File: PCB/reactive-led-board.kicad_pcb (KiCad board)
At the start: 2 copper layers, 2 parts, among them J1 Conn_01x03_Socket, U1 XIAO-ESP32-C5-SMD

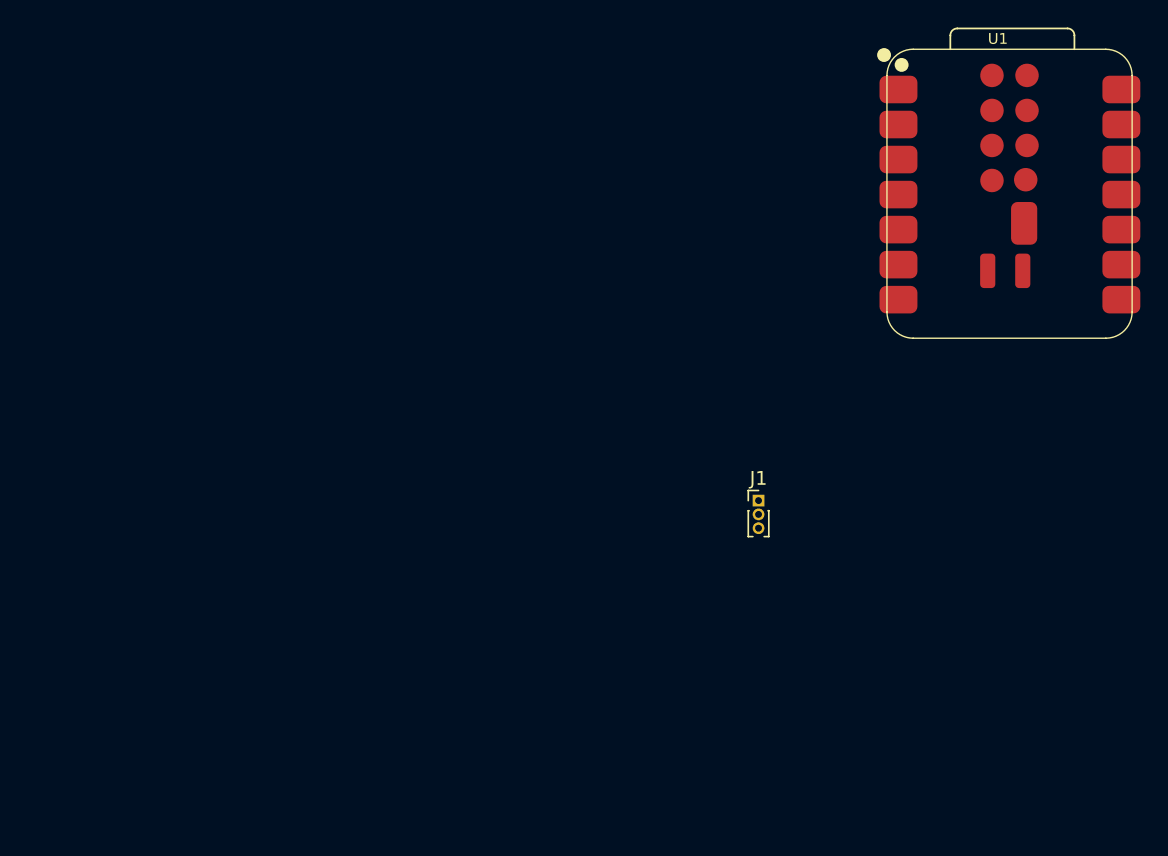
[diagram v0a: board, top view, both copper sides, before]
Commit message: routed the treaces and selected the parts i am going to use.
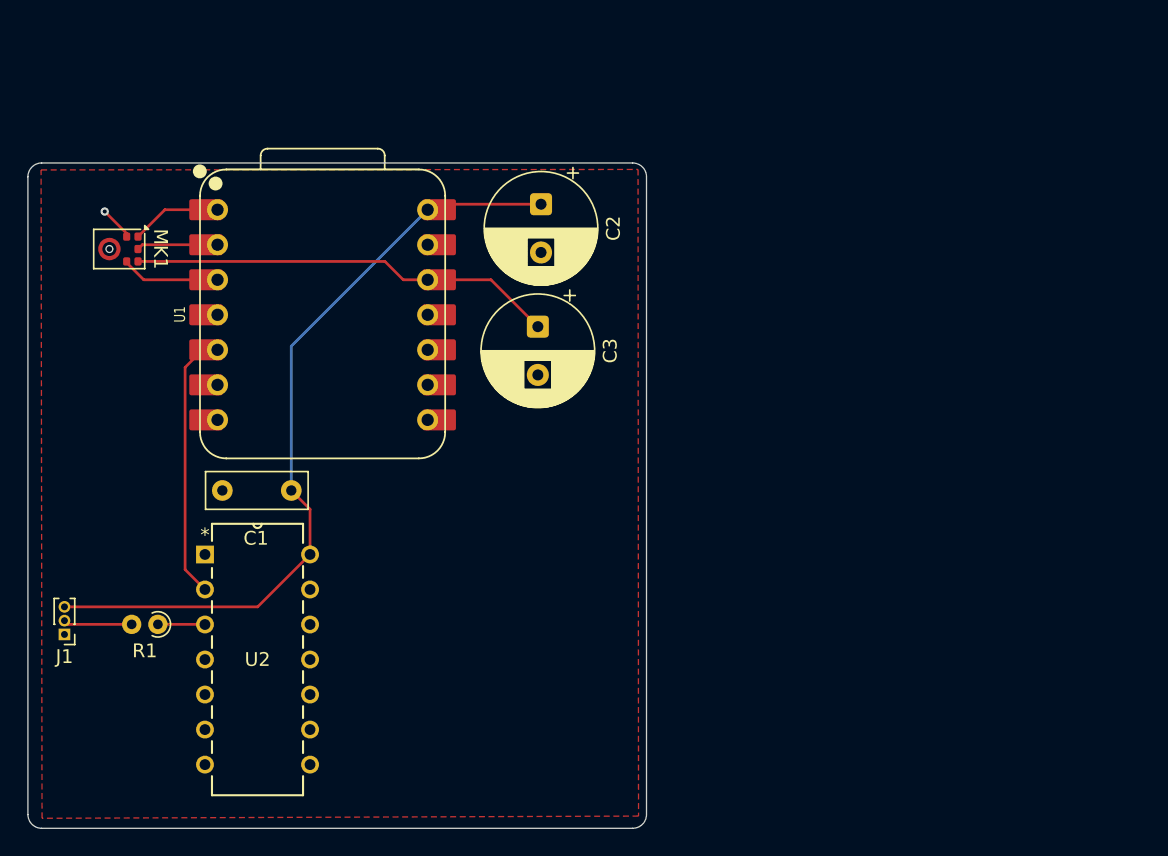
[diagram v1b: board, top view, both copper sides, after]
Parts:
- added C1: 100nF, Capacitor_THT:C_Rect_L7.2mm_W2.5mm_P5.00mm, F.Cu at (57.0, 56.2)
- added C2: 470uF, Capacitor_THT:CP_Radial_D8.0mm_P3.50mm, F.Cu at (75.1, 35.5)
- added C3: 470uF, Capacitor_THT:CP_Radial_D8.0mm_P3.50mm, F.Cu at (74.9, 44.4)
- added MK1: SPH0645LM4H, Sensor_Audio:Knowles_SPH0645LM4H-6_3.5x2.65mm, F.Cu at (44.5, 38.7)
- added R1: 62, Resistor_THT:R_Axial_DIN0204_L3.6mm_D1.6mm_P1.90mm_Vertical, F.Cu at (47.4, 65.9)
- added U2: SN74AHCT125N, sn74ahct125n:N14, F.Cu at (58.4, 76.1)
- U1: value XIAO-ESP32-C5-SMD -> XIAO-ESP32-S3-DIP; footprint Seeed Studio XIAO Series Library:XIAO-ESP32-C5-SMD -> Seeed Studio XIAO Series Library:XIAO-ESP32-S3-DIP
- moved J1 51.3 mm to (40.6, 66.7), turned to 180 degrees
- moved U1 41.0 mm to (59.3, 43.5), turned to 90 degrees
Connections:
- J1 pad 1: unconnected-(J1-Pin_1-Pad1) -> GND
- J1 pad 2: unconnected-(J1-Pin_2-Pad2) -> LED-DATA
- J1 pad 3: unconnected-(J1-Pin_3-Pad3) -> +5V
- U1 pad 1: unconnected-(U1-GPIO1_A0_D0-Pad1) -> WS
- U1 pad 12: unconnected-(U1-3V3-Pad12) -> +3V3
- U1 pad 13: unconnected-(U1-GND-Pad13) -> GND
- U1 pad 14: unconnected-(U1-VBUS-Pad14) -> +5V
- U1 pad 2: unconnected-(U1-GPIO0_D1-Pad2) -> DATA
- U1 pad 3: unconnected-(U1-GPIO25_D2-Pad3) -> BCLK
- U1 pad 5: unconnected-(U1-GPIO23_D4_SDA-Pad5) -> D4
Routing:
- net +5V: track 0.00 -> 57.4 mm
- net +3V3: track 0.00 -> 31.0 mm
- net D4: track 0.00 -> 19.6 mm
- net BCLK: track 0.00 -> 7.19 mm
- net WS: track 0.00 -> 6.57 mm
- net DATA: track 0.00 -> 5.89 mm
- net LED-DATA: track 0.00 -> 4.99 mm
- net Net-(U2-1Y): track 0.00 -> 3.42 mm
- net GND: track 0.00 -> 2.48 mm, vias 0 -> 1
- added copper zone on F.Cu, net GND
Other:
- board outline added: 44.9 x 48.3 mm

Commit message: added 3d model for the xiao and added the connector for the mic module
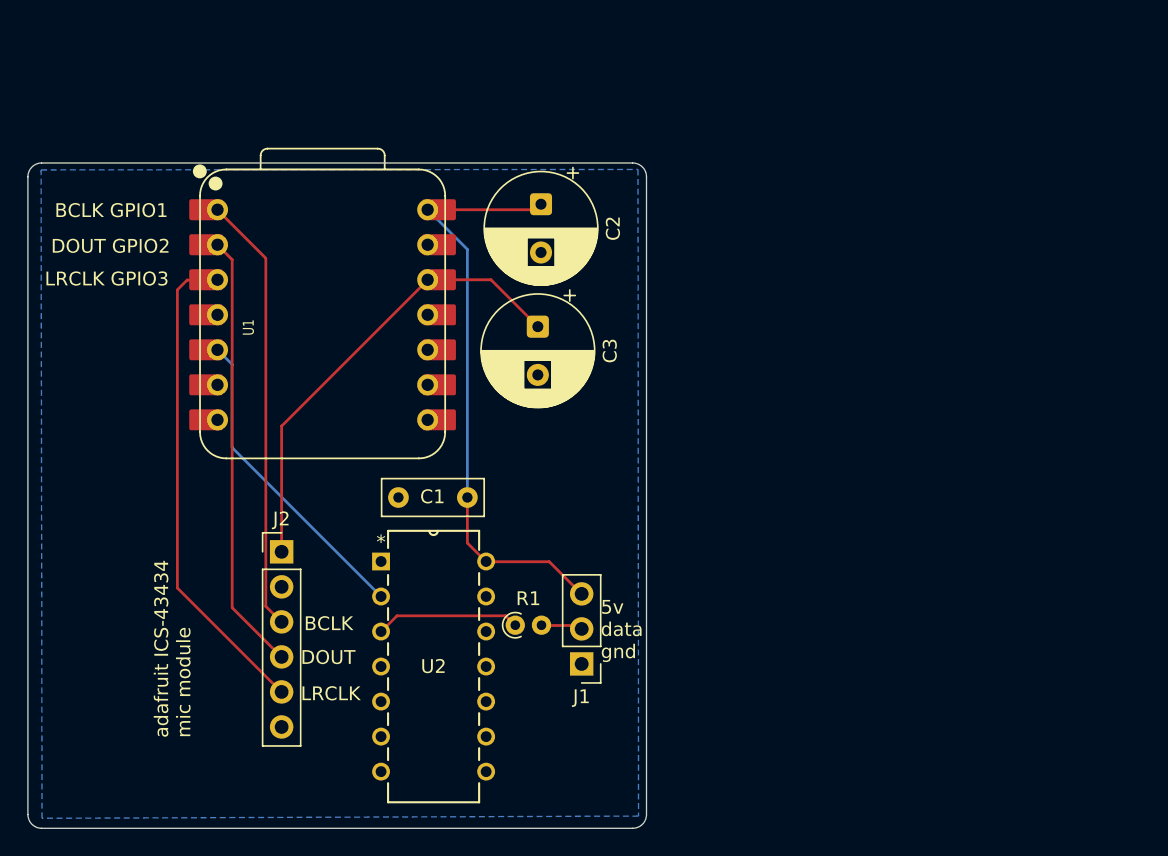
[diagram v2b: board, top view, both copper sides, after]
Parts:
- removed MK1: SPH0645LM4H, Sensor_Audio:Knowles_SPH0645LM4H-6_3.5x2.65mm
- added J2: Conn_01x06_Pin, Connector_PinHeader_2.54mm:PinHeader_1x06_P2.54mm_Vertical, F.Cu at (56.3, 60.7)
- J1: footprint Connector_PinHeader_1.00mm:PinHeader_1x03_P1.00mm_Vertical -> Connector_PinHeader_2.54mm:PinHeader_1x03_P2.54mm_Vertical
- moved J1 37.6 mm to (78.1, 68.8)
- moved R1 25.9 mm to (73.3, 66.0), turned to 0 degrees
- moved C1 12.8 mm to (69.8, 56.7)
- moved U2 12.8 mm to (71.2, 76.6)
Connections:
- U1 pad 1: WS -> BCLK
- U1 pad 2: DATA -> DOUT
- U1 pad 3: BCLK -> WS
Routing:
- net DOUT: track 0.00 -> 31.8 mm
- net WS: track 6.57 -> 35.5 mm
- net BCLK: track 7.19 -> 31.8 mm
- net +5V: track 57.4 -> 44.1 mm
- net Net-(U2-1Y): track 3.42 -> 10.5 mm
- net DATA: track 5.89 -> 0.00 mm
- net D4: track 19.6 -> 23.9 mm
- net +3V3: track 31.0 -> 33.5 mm
- net GND: track 2.48 -> 0.00 mm, vias 1 -> 0
- net LED-DATA: track 4.99 -> 3.03 mm
- added copper zone on B.Cu, net GND
- removed copper zone on F.Cu, net GND
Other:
- board text added: "5v data gnd"
- board text added: "BCLK"
- board text added: "BCLK GPIO1"
- board text added: "DOUT"
- board text added: "DOUT GPIO2"
- board text added: "LRCLK"
- board text added: "LRCLK GPIO3"
- board text added: "adafruit ICS-43434 mic module"

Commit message: did some hard ware changes and update bom swaped to using a screw terminal and updated the links in the bom to match with the leds i am going to use
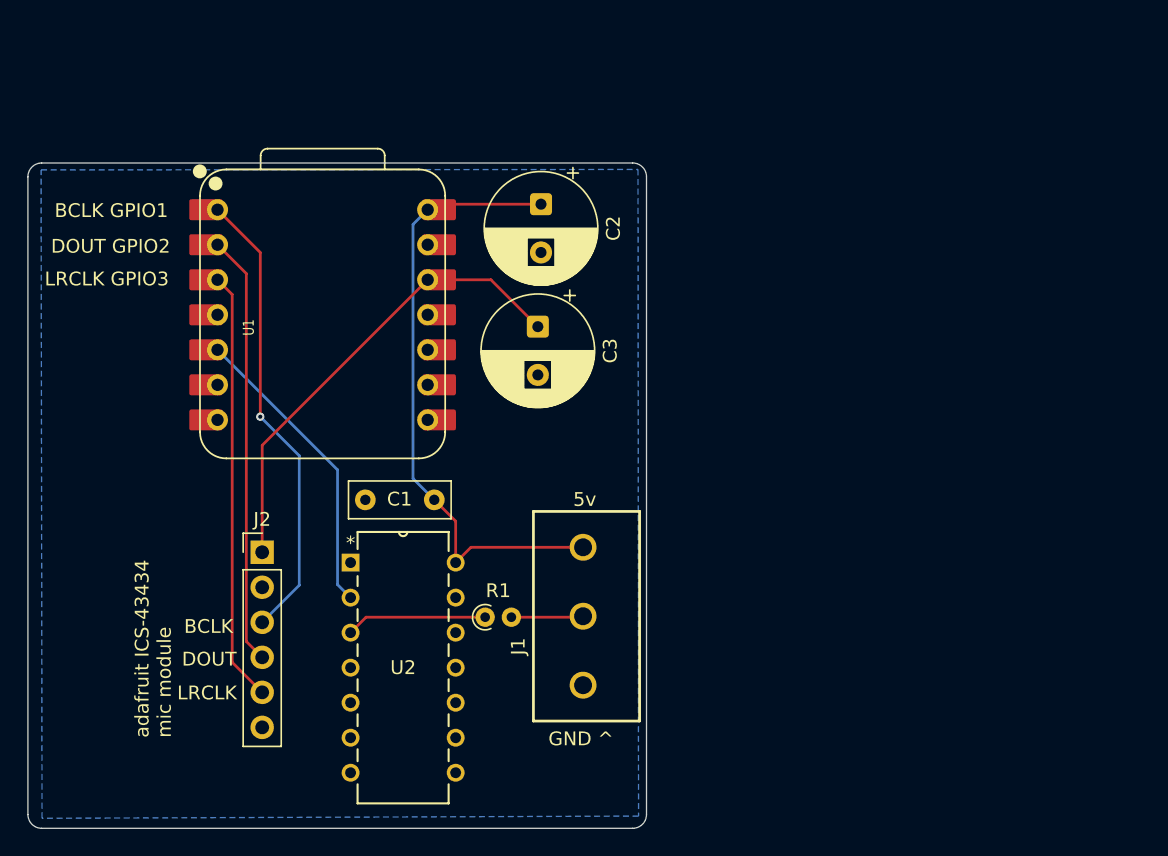
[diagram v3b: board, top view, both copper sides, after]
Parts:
- J1: footprint Connector_PinHeader_2.54mm:PinHeader_1x03_P2.54mm_Vertical -> custom_screw_terminals:691137710003
- moved J1 3.46 mm to (78.2, 65.3), turned to 90 degrees
- moved C1 2.41 mm to (67.4, 56.9)
- moved R1 2.26 mm to (71.1, 65.4)
- moved U2 2.21 mm to (69.0, 76.7)
- moved J2 1.41 mm to (54.9, 60.7)
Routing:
- net WS: track 35.5 -> 31.3 mm
- net LED-DATA: track 3.03 -> 5.23 mm
- net D4: track 23.9 -> 22.0 mm
- net BCLK: track 31.8 -> 33.5 mm, vias 0 -> 1
- net +5V: track 44.1 -> 45.4 mm
- net +3V3: track 33.5 -> 34.1 mm
- net DOUT: track 31.8 -> 31.3 mm
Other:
- board text added: "5v"
- board text added: "GND ^"
- board text removed: "5v data gnd"
